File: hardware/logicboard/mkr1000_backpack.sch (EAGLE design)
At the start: 2 parts, among them J4 DNP, J5 DNP

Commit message: Analog pins.
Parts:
- added ANALOG: (no value), SparkFun-Connectors:CONN_04X2
- added RN1: (no value), resistor-net:RN04
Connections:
- new net A0: ANALOG.1, J4.2, RN1.5
- new net A1: ANALOG.3, J4.3, RN1.4
- new net A2: ANALOG.5, J4.4, RN1.3
- new net A3: ANALOG.7, J4.5, RN1.2
- new net GND: J5.11, RN1.1
- new net VCC: ANALOG.2, ANALOG.4, ANALOG.6, ANALOG.8, J5.12

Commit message: First try.
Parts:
- added RN2: 10k, resistor-net:RN04
- ANALOG: device SparkFun-Connectors:CONN_04X2 -> con-ml:ML10L
- RN1: value (none) -> 10k
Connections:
- removed net A0: ANALOG.1, J4.2, RN1.5
- new net A4: ANALOG.8, J4.6, RN1.2
- new net A5: ANALOG.10, J4.7, RN2.5
- net A1: now also ANALOG.2, RN1.5; no longer ANALOG.3, RN1.4
- net A2: now also ANALOG.4, RN1.4; no longer ANALOG.5, RN1.3
- net A3: now also ANALOG.6, RN1.3; no longer ANALOG.7, RN1.2
- net GND: now also RN2.1
- net VCC: now also ANALOG.1, ANALOG.3, ANALOG.5, ANALOG.7, ANALOG.9; no longer ANALOG.2, ANALOG.4, ANALOG.6, ANALOG.8
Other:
- moved on the sheet: RN1

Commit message: Second try. Looks good.
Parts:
- J4, J5: device MK1_Zero:STRIP-14 -> SparkFun-Connectors:CONN_14
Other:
- moved on the sheet: J4, J5
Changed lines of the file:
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@@
 </classes>
 <parts>
-<part name="J5" library="MK1_Zero" deviceset="STRIP-14" device="" value="DNP"/>
-<part name="J4" library="MK1_Zero" deviceset="STRIP-14" device="" value="DNP"/>
+<part name="J5" library="SparkFun-Connectors" library_urn="urn:adsk.eagle:library:513" deviceset="CONN_14" device="" package3d_urn="urn:adsk.eagle:package:38183/1" value="DNP"/>
+<part name="J4" library="SparkFun-Connectors" library_urn="urn:adsk.eagle:library:513" deviceset="CONN_14" device="" package3d_urn="urn:adsk.eagle:package:38183/1" value="DNP"/>
 <part name="FRAME1" library="frames" deviceset="A3L-LOC" device="" value="Page 1"/>
 <part name="FRAME2" library="frames" deviceset="A3L-LOC" device="" value="Page 2"/>
@@
 </plain>
 <instances>
-<instance part="J5" gate="G$1" x="297.18" y="116.84" smashed="yes">
-<attribute name="VALUE" x="297.18" y="96.012" size="1.778" layer="96" align="top-left" display="off"/>
-<attribute name="NAME" x="297.942" y="135.128" size="1.778" layer="95"/>
+<instance part="J5" gate="G$1" x="294.64" y="116.84" smashed="yes">
+<attribute name="VALUE" x="294.64" y="96.012" size="1.778" layer="96" align="top-left" display="off"/>
+<attribute name="NAME" x="295.402" y="135.128" size="1.778" layer="95"/>
 </instance>
-<instance part="J4" gate="G$1" x="279.4" y="114.3" smashed="yes" rot="R180">
-<attribute name="VALUE" x="279.4" y="135.128" size="1.778" layer="96" rot="R180" align="top-left" display="off"/>
-<attribute name="NAME" x="276.352" y="135.128" size="1.778" layer="95"/>
+<instance part="J4" gate="G$1" x="281.94" y="114.3" smashed="yes" rot="R180">
+<attribute name="VALUE" x="281.94" y="135.128" size="1.778" layer="96" rot="R180" align="top-left" display="off"/>
+<attribute name="NAME" x="278.892" y="135.128" size="1.778" layer="95"/>
 </instance>
 <instance part="FRAME1" gate="G$1" x="0" y="0"/>

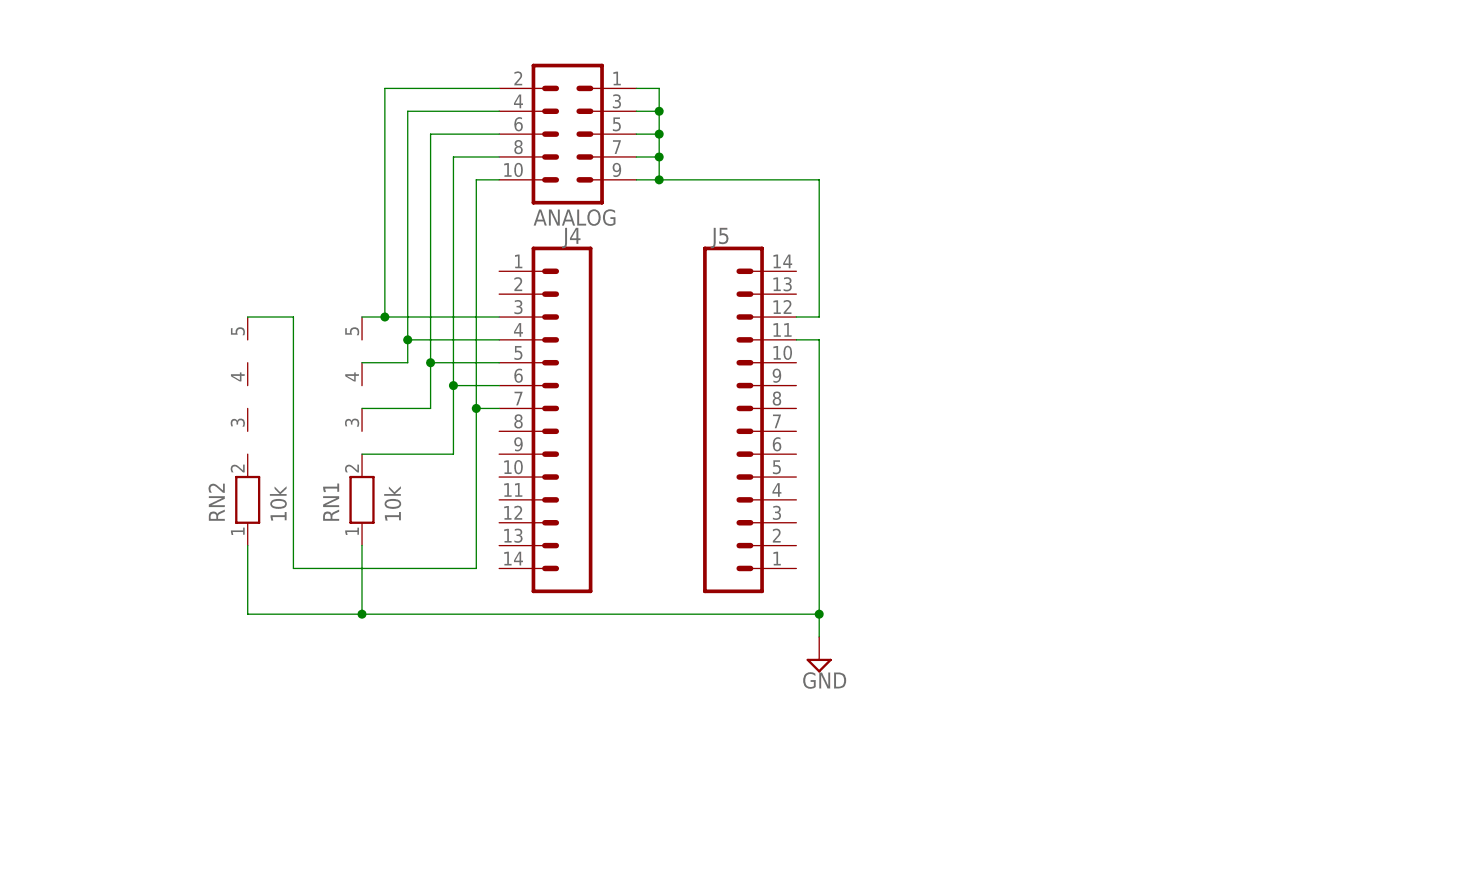
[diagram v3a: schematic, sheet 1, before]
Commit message: Added encoder switch for selecting IP address.
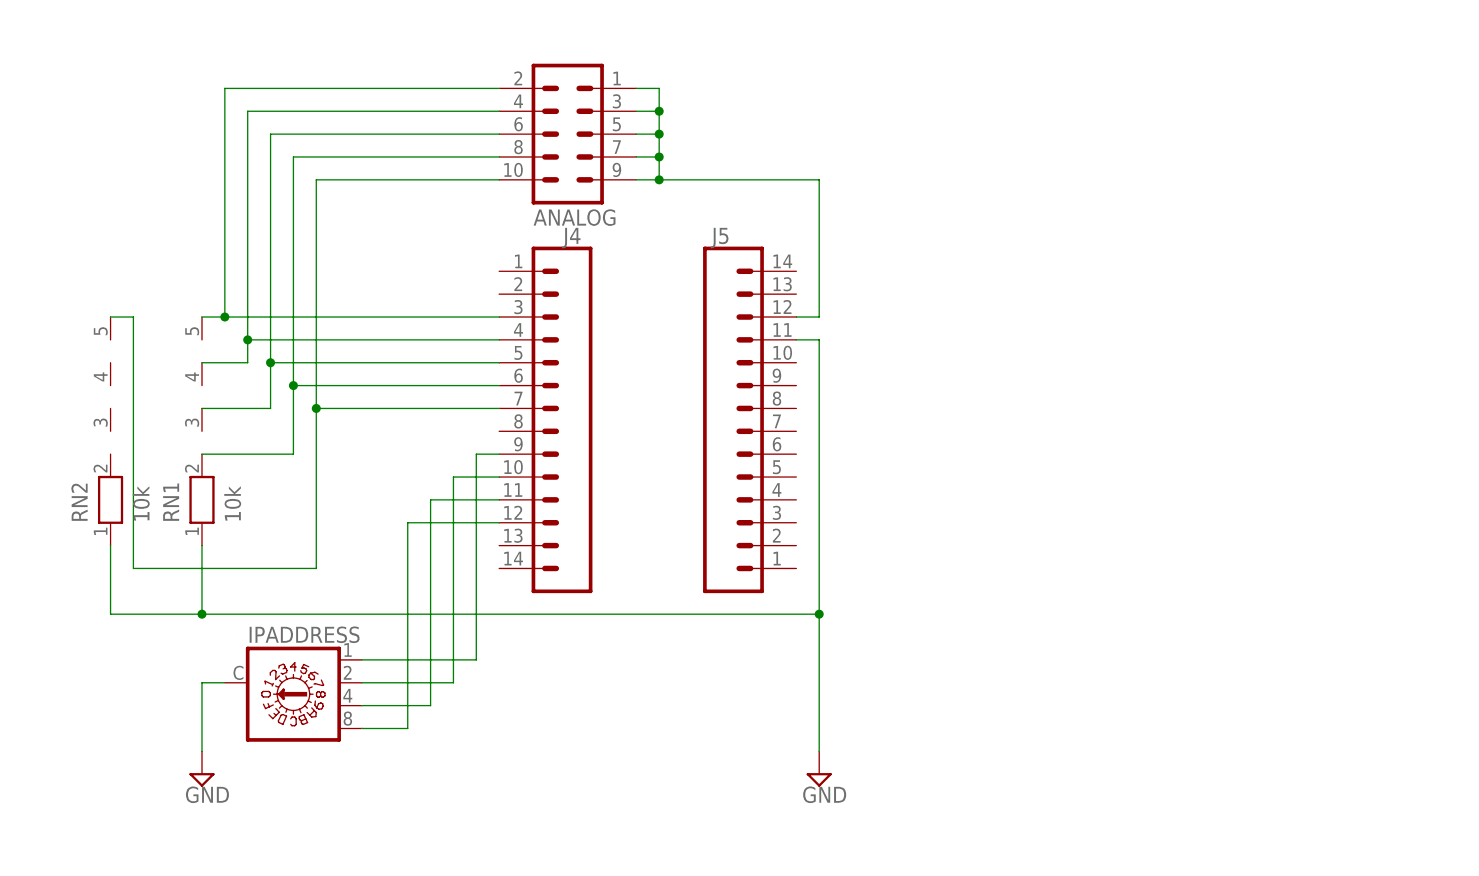
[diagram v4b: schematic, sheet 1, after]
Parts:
- added IPADDRESS: (no value), switch-dil:A1353HEX
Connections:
- new net D0: IPADDRESS.1, J4.9
- new net D1: IPADDRESS.2, J4.10
- new net D2: IPADDRESS.4, J4.11
- new net D3: IPADDRESS.8, J4.12
- net GND: now also IPADDRESS.C
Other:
- moved on the sheet: RN1, RN2
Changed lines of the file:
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@@
 <part name="ANALOG" library="con-ml" library_urn="urn:adsk.eagle:library:164" deviceset="ML10L" device="" package3d_urn="urn:adsk.eagle:package:8678/1"/>
 <part name="RN2" library="resistor-net" library_urn="urn:adsk.eagle:library:343" deviceset="RN04" device="" package3d_urn="urn:adsk.eagle:package:24976/1" value="10k"/>
+<part name="IPADDRESS" library="switch-dil" library_urn="urn:adsk.eagle:library:375" deviceset="A1353HEX" device="" package3d_urn="urn:adsk.eagle:package:27207/1"/>
+<part name="SUPPLY2" library="supply2" library_urn="urn:adsk.eagle:library:372" deviceset="GND" device=""/>
 </parts>
 <sheets>
@@
 </instance>
 <instance part="FRAME1" gate="G$1" x="0" y="0"/>
-<instance part="RN1" gate="1" x="256.54" y="106.68" rot="R90"/>
-<instance part="SUPPLY1" gate="GND" x="307.34" y="88.9"/>
+<instance part="RN1" gate="1" x="238.76" y="106.68" rot="R90"/>
+<instance part="SUPPLY1" gate="GND" x="307.34" y="76.2"/>
 <instance part="ANALOG" gate="1" x="279.4" y="147.32" rot="MR180"/>
-<instance part="RN2" gate="1" x="243.84" y="106.68" rot="R90"/>
+<instance part="RN2" gate="1" x="228.6" y="106.68" rot="R90"/>
+<instance part="IPADDRESS" gate="1" x="248.92" y="86.36" rot="R270"/>
+<instance part="SUPPLY2" gate="GND" x="238.76" y="76.2"/>
 </instances>
 <busses>
@@
 <net name="A1" class="0">
 <segment>
-<wire x1="271.78" y1="152.4" x2="259.08" y2="152.4" width="0.1524" layer="91"/>
-<wire x1="259.08" y1="152.4" x2="259.08" y2="127" width="0.1524" layer="91"/>
+<wire x1="271.78" y1="152.4" x2="241.3" y2="152.4" width="0.1524" layer="91"/>
+<wire x1="241.3" y1="152.4" x2="241.3" y2="127" width="0.1524" layer="91"/>
 <pinref part="ANALOG" gate="1" pin="2"/>
 <pinref part="J4" gate="G$1" pin="3"/>
-<wire x1="271.78" y1="127" x2="259.08" y2="127" width="0.1524" layer="91"/>
+<wire x1="271.78" y1="127" x2="241.3" y2="127" width="0.1524" layer="91"/>
 <pinref part="RN1" gate="1" pin="5"/>
-<wire x1="259.08" y1="127" x2="256.54" y2="127" width="0.1524" layer="91"/>
-<junction x="259.08" y="127"/>
+<wire x1="241.3" y1="127" x2="238.76" y2="127" width="0.1524" layer="91"/>
+<junction x="241.3" y="127"/>
 </segment>
 </net>
 <net name="A2" class="0">
 <segment>
-<wire x1="271.78" y1="149.86" x2="261.62" y2="149.86" width="0.1524" layer="91"/>
+<wire x1="271.78" y1="149.86" x2="243.84" y2="149.86" width="0.1524" layer="91"/>
 <pinref part="ANALOG" gate="1" pin="4"/>
 <pinref part="J4" gate="G$1" pin="4"/>
-<wire x1="271.78" y1="124.46" x2="261.62" y2="124.46" width="0.1524" layer="91"/>
-<wire x1="261.62" y1="121.92" x2="261.62" y2="124.46" width="0.1524" layer="91"/>
+<wire x1="271.78" y1="124.46" x2="243.84" y2="124.46" width="0.1524" layer="91"/>
+<wire x1="243.84" y1="121.92" x2="243.84" y2="124.46" width="0.1524" layer="91"/>
 <pinref part="RN1" gate="1" pin="4"/>
-<wire x1="256.54" y1="121.92" x2="261.62" y2="121.92" width="0.1524" layer="91"/>
-<wire x1="261.62" y1="149.86" x2="261.62" y2="124.46" width="0.1524" layer="91"/>
-<junction x="261.62" y="124.46"/>
+<wire x1="238.76" y1="121.92" x2="243.84" y2="121.92" width="0.1524" layer="91"/>
+<wire x1="243.84" y1="149.86" x2="243.84" y2="124.46" width="0.1524" layer="91"/>
+<junction x="243.84" y="124.46"/>
 </segment>
 </net>
 <net name="A3" class="0">
 <segment>
-<wire x1="271.78" y1="147.32" x2="264.16" y2="147.32" width="0.1524" layer="91"/>
+<wire x1="271.78" y1="147.32" x2="246.38" y2="147.32" width="0.1524" layer="91"/>
 <pinref part="ANALOG" gate="1" pin="6"/>
 <pinref part="J4" gate="G$1" pin="5"/>
-<wire x1="271.78" y1="121.92" x2="264.16" y2="121.92" width="0.1524" layer="91"/>
-<wire x1="264.16" y1="116.84" x2="264.16" y2="121.92" width="0.1524" layer="91"/>
+<wire x1="271.78" y1="121.92" x2="246.38" y2="121.92" width="0.1524" layer="91"/>
+<wire x1="246.38" y1="116.84" x2="246.38" y2="121.92" width="0.1524" layer="91"/>
 <pinref part="RN1" gate="1" pin="3"/>
-<wire x1="256.54" y1="116.84" x2="264.16" y2="116.84" width="0.1524" layer="91"/>
-<wire x1="264.16" y1="147.32" x2="264.16" y2="121.92" width="0.1524" layer="91"/>
-<junction x="264.16" y="121.92"/>
+<wire x1="238.76" y1="116.84" x2="246.38" y2="116.84" width="0.1524" layer="91"/>
+<wire x1="246.38" y1="147.32" x2="246.38" y2="121.92" width="0.1524" layer="91"/>
+<junction x="246.38" y="121.92"/>
 </segment>
 </net>
 <net name="A4" class="0">
 <segment>
-<wire x1="271.78" y1="144.78" x2="266.7" y2="144.78" width="0.1524" layer="91"/>
+<wire x1="271.78" y1="144.78" x2="248.92" y2="144.78" width="0.1524" layer="91"/>
 <pinref part="ANALOG" gate="1" pin="8"/>
 <pinref part="J4" gate="G$1" pin="6"/>
-<wire x1="271.78" y1="119.38" x2="266.7" y2="119.38" width="0.1524" layer="91"/>
-<wire x1="266.7" y1="111.76" x2="266.7" y2="119.38" width="0.1524" layer="91"/>
+<wire x1="271.78" y1="119.38" x2="248.92" y2="119.38" width="0.1524" layer="91"/>
+<wire x1="248.92" y1="111.76" x2="248.92" y2="119.38" width="0.1524" layer="91"/>
 <pinref part="RN1" gate="1" pin="2"/>
-<wire x1="256.54" y1="111.76" x2="266.7" y2="111.76" width="0.1524" layer="91"/>
-<wire x1="266.7" y1="144.78" x2="266.7" y2="119.38" width="0.1524" layer="91"/>
-<junction x="266.7" y="119.38"/>
+<wire x1="238.76" y1="111.76" x2="248.92" y2="111.76" width="0.1524" layer="91"/>
+<wire x1="248.92" y1="144.78" x2="248.92" y2="119.38" width="0.1524" layer="91"/>
+<junction x="248.92" y="119.38"/>
 </segment>
 </net>
@@
 <wire x1="304.8" y1="124.46" x2="307.34" y2="124.46" width="0.1524" layer="91"/>
 <wire x1="307.34" y1="124.46" x2="307.34" y2="93.98" width="0.1524" layer="91"/>
-<wire x1="307.34" y1="93.98" x2="256.54" y2="93.98" width="0.1524" layer="91"/>
+<wire x1="307.34" y1="93.98" x2="238.76" y2="93.98" width="0.1524" layer="91"/>
 <pinref part="RN1" gate="1" pin="1"/>
-<wire x1="256.54" y1="93.98" x2="256.54" y2="101.6" width="0.1524" layer="91"/>
+<wire x1="238.76" y1="93.98" x2="238.76" y2="101.6" width="0.1524" layer="91"/>
 <pinref part="SUPPLY1" gate="GND" pin="GND"/>
-<wire x1="307.34" y1="93.98" x2="307.34" y2="91.44" width="0.1524" layer="91"/>
+<wire x1="307.34" y1="93.98" x2="307.34" y2="78.74" width="0.1524" layer="91"/>
 <junction x="307.34" y="93.98"/>
 <pinref part="RN2" gate="1" pin="1"/>
-<wire x1="243.84" y1="101.6" x2="243.84" y2="93.98" width="0.1524" layer="91"/>
-<wire x1="243.84" y1="93.98" x2="256.54" y2="93.98" width="0.1524" layer="91"/>
-<junction x="256.54" y="93.98"/>
+<wire x1="228.6" y1="101.6" x2="228.6" y2="93.98" width="0.1524" layer="91"/>
+<wire x1="228.6" y1="93.98" x2="238.76" y2="93.98" width="0.1524" layer="91"/>
+<junction x="238.76" y="93.98"/>
+</segment>
+<segment>
+<pinref part="IPADDRESS" gate="1" pin="C"/>
+<wire x1="241.3" y1="86.36" x2="238.76" y2="86.36" width="0.1524" layer="91"/>
+<pinref part="SUPPLY2" gate="GND" pin="GND"/>
+<wire x1="238.76" y1="86.36" x2="238.76" y2="78.74" width="0.1524" layer="91"/>
 </segment>
 </net>
@@
 <net name="A5" class="0">
 <segment>
-<wire x1="269.24" y1="116.84" x2="269.24" y2="99.06" width="0.1524" layer="91"/>
-<wire x1="269.24" y1="99.06" x2="248.92" y2="99.06" width="0.1524" layer="91"/>
-<wire x1="248.92" y1="99.06" x2="248.92" y2="127" width="0.1524" layer="91"/>
+<wire x1="251.46" y1="116.84" x2="251.46" y2="99.06" width="0.1524" layer="91"/>
+<wire x1="251.46" y1="99.06" x2="231.14" y2="99.06" width="0.1524" layer="91"/>
+<wire x1="231.14" y1="99.06" x2="231.14" y2="127" width="0.1524" layer="91"/>
 <pinref part="RN2" gate="1" pin="5"/>
-<wire x1="248.92" y1="127" x2="243.84" y2="127" width="0.1524" layer="91"/>
+<wire x1="231.14" y1="127" x2="228.6" y2="127" width="0.1524" layer="91"/>
 <pinref part="J4" gate="G$1" pin="7"/>
-<wire x1="271.78" y1="116.84" x2="269.24" y2="116.84" width="0.1524" layer="91"/>
+<wire x1="271.78" y1="116.84" x2="251.46" y2="116.84" width="0.1524" layer="91"/>
 <pinref part="ANALOG" gate="1" pin="10"/>
-<wire x1="271.78" y1="142.24" x2="269.24" y2="142.24" width="0.1524" layer="91"/>
-<wire x1="269.24" y1="142.24" x2="269.24" y2="116.84" width="0.1524" layer="91"/>
-<junction x="269.24" y="116.84"/>
+<wire x1="271.78" y1="142.24" x2="251.46" y2="142.24" width="0.1524" layer="91"/>
+<wire x1="251.46" y1="142.24" x2="251.46" y2="116.84" width="0.1524" layer="91"/>
+<junction x="251.46" y="116.84"/>
 </segment>
 </net>
+<net name="D0" class="0">
+<segment>
+<pinref part="J4" gate="G$1" pin="9"/>
+<wire x1="271.78" y1="111.76" x2="269.24" y2="111.76" width="0.1524" layer="91"/>
+<wire x1="269.24" y1="111.76" x2="269.24" y2="88.9" width="0.1524" layer="91"/>
+<pinref part="IPADDRESS" gate="1" pin="1"/>
+<wire x1="269.24" y1="88.9" x2="256.54" y2="88.9" width="0.1524" layer="91"/>
+</segment>
+</net>
+<net name="D1" class="0">
+<segment>
+<pinref part="J4" gate="G$1" pin="10"/>
+<wire x1="271.78" y1="109.22" x2="266.7" y2="109.22" width="0.1524" layer="91"/>
+<wire x1="266.7" y1="109.22" x2="266.7" y2="86.36" width="0.1524" layer="91"/>
+<pinref part="IPADDRESS" gate="1" pin="2"/>
+<wire x1="266.7" y1="86.36" x2="256.54" y2="86.36" width="0.1524" layer="91"/>
+</segment>
+</net>
+<net name="D2" class="0">
+<segment>
+<pinref part="J4" gate="G$1" pin="11"/>
+<wire x1="271.78" y1="106.68" x2="264.16" y2="106.68" width="0.1524" layer="91"/>
+<wire x1="264.16" y1="106.68" x2="264.16" y2="83.82" width="0.1524" layer="91"/>
+<pinref part="IPADDRESS" gate="1" pin="4"/>
+<wire x1="264.16" y1="83.82" x2="256.54" y2="83.82" width="0.1524" layer="91"/>
+</segment>
+</net>
+<net name="D3" class="0">
+<segment>
+<pinref part="J4" gate="G$1" pin="12"/>
+<wire x1="271.78" y1="104.14" x2="261.62" y2="104.14" width="0.1524" layer="91"/>
+<wire x1="261.62" y1="104.14" x2="261.62" y2="81.28" width="0.1524" layer="91"/>
+<pinref part="IPADDRESS" gate="1" pin="8"/>
+<wire x1="261.62" y1="81.28" x2="256.54" y2="81.28" width="0.1524" layer="91"/>
+</segment>
+</net>

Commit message: Capacitor.
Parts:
- added C1: 0.1u, resistor:C-US025-025X050
- ANALOG: device con-ml:ML10L -> con-ml:ML14L
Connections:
- new net A0: ANALOG.2, J4.2, RN1.5
- new net A6: ANALOG.14, J4.8, RN2.3
- net A1: now also ANALOG.4, RN1.4; no longer ANALOG.2, RN1.5
- net A2: now also ANALOG.6, RN1.3; no longer ANALOG.4, RN1.4
- net A3: now also ANALOG.8, RN1.2; no longer ANALOG.6, RN1.3
- net A4: now also ANALOG.10, RN2.5; no longer ANALOG.8, RN1.2
- net A5: now also ANALOG.12, RN2.4; no longer ANALOG.10, RN2.5
- net GND: now also C1.2
- net VCC: now also ANALOG.11, ANALOG.13, C1.1
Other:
- moved on the sheet: RN1, RN2
